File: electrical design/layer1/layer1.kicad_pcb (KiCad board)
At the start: 2 copper layers, 178 x 169.1 mm, 191 parts, among them J1 XT60-F, J2 1x07 2.54 FEMALE, J3 1x07 2.54 FEMALE, Q1 MOSFET-NCH-FQP30N06L, Q2 MOSFET-NCH-AO3404A, SW1 SW_DPDT_x2, U1 CD74HC4067SM, U2 CD74HC4067SM

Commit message: update layer 1 pcb
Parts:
- removed the C33 at (235.0, 105.0)
- removed the C33 at (-20.5, 99.5)
- removed the C34 at (224.9, 114.3)
- removed the C34 at (-19.5, 120.5)
- removed the C35 at (228.9, 115.0)
- removed the C36 at (250.7, 90.6)
- removed D33: 1N4728, Diode_THT:D_DO-41_SOD81_P10.16mm_Horizontal
- removed D34: 1N5401, Diode_THT:D_DO-27_P15.24mm_Horizontal
- removed J1, SOLENOID1: XT60-F, Connector_AMASS:AMASS_XT30UPB-F_1x02_P5.0mm_Vertical
- removed the R33 at (107.2, 57.8)
- removed the R33 at (-19.5, 122.2)
- removed the R35 at (-19.5, 124.0)
- removed the R35 at (156.0, 160.8)
- added C33: 1000µF/63V, Capacitor_THT:CP_Radial_D16.0mm_P7.50mm, F.Cu at (28.0, 89.2)
- added C34: 1500pF, Capacitor_SMD:C_0603_1608Metric, F.Cu at (28.5, 113.8)
- added H1: MountingHole, MountingHole:MountingHole_3.2mm_M3_Pad, F.Cu at (186.0, 44.0)
- added H10: MountingHole, MountingHole:MountingHole_3.2mm_M3_Pad, F.Cu at (209.8, 36.8)
- added H11: MountingHole, MountingHole:MountingHole_3.2mm_M3_Pad, F.Cu at (201.9, 52.6)
- added H12: MountingHole, MountingHole:MountingHole_3.2mm_M3_Pad, F.Cu at (217.8, 36.8)
- added H13: MountingHole, MountingHole:MountingHole_3.2mm_M3_Pad, F.Cu at (198.2, 28.8)
- added H14: MountingHole, MountingHole:MountingHole_3.2mm_M3_Pad, F.Cu at (222.1, 28.8)
- added H15: MountingHole, MountingHole:MountingHole_3.2mm_M3_Pad, F.Cu at (186.0, 36.0)
- added H16: MountingHole, MountingHole:MountingHole_3.2mm_M3_Pad, F.Cu at (193.9, 36.8)
- added H17: MountingHole, MountingHole:MountingHole_3.2mm_M3_Pad, F.Cu at (217.8, 44.7)
- added H18: MountingHole, MountingHole:MountingHole_3.2mm_M3_Pad, F.Cu at (214.2, 28.8)
- added H19: MountingHole, MountingHole:MountingHole_3.2mm_M3_Pad, F.Cu at (193.9, 52.6)
- added H2: MountingHole, MountingHole:MountingHole_3.2mm_M3_Pad, F.Cu at (186.0, 52.0)
- added H20: MountingHole, MountingHole:MountingHole_3.2mm_M3_Pad, F.Cu at (201.9, 44.7)
- added H21: MountingHole, MountingHole:MountingHole_3.2mm_M3_Pad, F.Cu at (201.9, 36.8)
- added H22: MountingHole, MountingHole:MountingHole_3.2mm_M3_Pad, F.Cu at (209.8, 52.6)
- added H3: MountingHole, MountingHole:MountingHole_3.2mm_M3_Pad, F.Cu at (230.1, 28.8)
- added H4: MountingHole, MountingHole:MountingHole_3.2mm_M3_Pad, F.Cu at (238.0, 28.8)
- added H5: MountingHole, MountingHole:MountingHole_3.2mm_M3_Pad, F.Cu at (206.2, 28.8)
- added H6: MountingHole, MountingHole:MountingHole_3.2mm_M3_Pad, F.Cu at (225.8, 36.8)
- added H7: MountingHole, MountingHole:MountingHole_3.2mm_M3_Pad, F.Cu at (217.8, 52.6)
- added H8: MountingHole, MountingHole:MountingHole_3.2mm_M3_Pad, F.Cu at (209.8, 44.7)
- added H9: MountingHole, MountingHole:MountingHole_3.2mm_M3_Pad, F.Cu at (72.1, 59.1)
- added J4: XT30PW-F, Connector_AMASS:AMASS_XT30PW-F_1x02_P2.50mm_Horizontal, F.Cu at (43.4, 102.5)
- added R33: 20, Resistor_SMD:R_0603_1608Metric, F.Cu at (28.5, 115.5)
- added R35: 10k, Resistor_SMD:R_0603_1608Metric, F.Cu at (28.5, 117.2)
- C35: renamed from C36; moved to B.Cu
- C36: renamed from C37; moved to B.Cu
- R36, R37, R38, R39, U1, U2: moved to B.Cu
- moved D2 196.8 mm to (35.0, 104.8), turned to -90 degrees
- moved D1 172.7 mm to (38.5, 104.1), turned to 90 degrees
- moved C36 64.5 mm to (143.5, 100.8), turned to -90 degrees
- moved C35 64.2 mm to (67.0, 109.3), turned to 90 degrees
- moved R38 52.5 mm to (143.5, 109.2), turned to 90 degrees
- moved R36 51.8 mm to (67.0, 100.5), turned to -90 degrees
- moved Q1 46.4 mm to (29.0, 109.8), turned to 90 degrees
- moved U2 45.8 mm to (134.5, 105.0), turned to 90 degrees
- moved U1 45.5 mm to (76.0, 105.0), turned to -90 degrees
- moved J2 43.8 mm to (230.8, 98.9)
- moved J3 43.8 mm to (230.8, 115.1)
- moved SW1 43.8 mm to (226.8, 120.0)
- moved R39 37.3 mm to (123.5, 100.0), turned to 180 degrees
- moved R37 37.0 mm to (87.0, 110.0), turned to 0 degrees
- moved R34 35.5 mm to (28.5, 119.0)
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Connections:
- D1 pad 2: /SOLENOIDPOWER -> +48V
- LDR10 pad 1: unconnected-(LDR10-Pad1) -> VCCQ
- LDR11 pad 1: unconnected-(LDR11-Pad1) -> VCCQ
- LDR12 pad 1: unconnected-(LDR12-Pad1) -> VCCQ
- LDR13 pad 1: unconnected-(LDR13-Pad1) -> VCCQ
- LDR14 pad 1: unconnected-(LDR14-Pad1) -> VCCQ
- LDR15 pad 1: unconnected-(LDR15-Pad1) -> VCCQ
- LDR16 pad 1: unconnected-(LDR16-Pad1) -> VCCQ
- LDR17 pad 1: unconnected-(LDR17-Pad1) -> VCCQ
- LDR17 pad 2: unconnected-(LDR17-Pad2) -> Net-(LDR17-Pad2)
- LDR18 pad 1: unconnected-(LDR18-Pad1) -> VCCQ
- LDR18 pad 2: unconnected-(LDR18-Pad2) -> Net-(LDR18-Pad2)
- LDR19 pad 1: unconnected-(LDR19-Pad1) -> VCCQ
- LDR19 pad 2: unconnected-(LDR19-Pad2) -> Net-(LDR19-Pad2)
- LDR20 pad 1: unconnected-(LDR20-Pad1) -> VCCQ
- LDR20 pad 2: unconnected-(LDR20-Pad2) -> Net-(LDR20-Pad2)
- LDR21 pad 1: unconnected-(LDR21-Pad1) -> VCCQ
- LDR21 pad 2: unconnected-(LDR21-Pad2) -> Net-(LDR21-Pad2)
- LDR22 pad 1: unconnected-(LDR22-Pad1) -> VCCQ
- LDR22 pad 2: unconnected-(LDR22-Pad2) -> Net-(LDR22-Pad2)
- LDR23 pad 1: unconnected-(LDR23-Pad1) -> VCCQ
- LDR23 pad 2: unconnected-(LDR23-Pad2) -> Net-(LDR23-Pad2)
- LDR24 pad 1: unconnected-(LDR24-Pad1) -> VCCQ
- LDR24 pad 2: unconnected-(LDR24-Pad2) -> Net-(LDR24-Pad2)
- LDR25 pad 1: unconnected-(LDR25-Pad1) -> VCCQ
- LDR25 pad 2: unconnected-(LDR25-Pad2) -> Net-(LDR25-Pad2)
- LDR26 pad 1: unconnected-(LDR26-Pad1) -> VCCQ
- LDR26 pad 2: unconnected-(LDR26-Pad2) -> Net-(LDR26-Pad2)
- LDR27 pad 1: unconnected-(LDR27-Pad1) -> VCCQ
- LDR27 pad 2: unconnected-(LDR27-Pad2) -> Net-(LDR27-Pad2)
- LDR28 pad 1: unconnected-(LDR28-Pad1) -> VCCQ
- LDR28 pad 2: unconnected-(LDR28-Pad2) -> Net-(LDR28-Pad2)
- LDR29 pad 1: unconnected-(LDR29-Pad1) -> VCCQ
- LDR29 pad 2: unconnected-(LDR29-Pad2) -> Net-(LDR29-Pad2)
- LDR30 pad 1: unconnected-(LDR30-Pad1) -> VCCQ
- LDR30 pad 2: unconnected-(LDR30-Pad2) -> Net-(LDR30-Pad2)
- LDR31 pad 1: unconnected-(LDR31-Pad1) -> VCCQ
- LDR31 pad 2: unconnected-(LDR31-Pad2) -> Net-(LDR31-Pad2)
- LDR32 pad 1: unconnected-(LDR32-Pad1) -> VCCQ
- LDR32 pad 2: unconnected-(LDR32-Pad2) -> Net-(LDR32-Pad2)
- LDR9 pad 1: unconnected-(LDR9-Pad1) -> VCCQ
- R34 pad 1: Net-(R34-Pad1) -> +12V
- U1 pad 16: unconnected-(U1-Pad16) -> Net-(LDR16-Pad2)
- U1 pad 17: unconnected-(U1-Pad17) -> Net-(LDR15-Pad2)
- U1 pad 18: unconnected-(U1-Pad18) -> Net-(LDR14-Pad2)
- U1 pad 19: unconnected-(U1-Pad19) -> Net-(LDR13-Pad2)
- U1 pad 2: Net-(LDR1-Pad2) -> Net-(LDR8-Pad2)
- U1 pad 20: unconnected-(U1-Pad20) -> Net-(LDR12-Pad2)
- U1 pad 21: unconnected-(U1-Pad21) -> Net-(LDR11-Pad2)
- U1 pad 22: unconnected-(U1-Pad22) -> Net-(LDR10-Pad2)
- U1 pad 23: unconnected-(U1-Pad23) -> Net-(LDR9-Pad2)
- U1 pad 3: Net-(LDR2-Pad2) -> Net-(LDR7-Pad2)
- U1 pad 4: Net-(LDR3-Pad2) -> Net-(LDR6-Pad2)
- U1 pad 5: Net-(LDR4-Pad2) -> Net-(LDR5-Pad2)
- U1 pad 6: Net-(LDR5-Pad2) -> Net-(LDR4-Pad2)
- U1 pad 7: Net-(LDR6-Pad2) -> Net-(LDR3-Pad2)
- U1 pad 8: Net-(LDR7-Pad2) -> Net-(LDR2-Pad2)
- U1 pad 9: Net-(LDR8-Pad2) -> Net-(LDR1-Pad2)
- U2 pad 16: Net-(LDR9-Pad2) -> Net-(LDR32-Pad2)
- U2 pad 17: Net-(LDR10-Pad2) -> Net-(LDR31-Pad2)
- U2 pad 18: Net-(LDR11-Pad2) -> Net-(LDR30-Pad2)
- U2 pad 19: Net-(LDR12-Pad2) -> Net-(LDR29-Pad2)
- U2 pad 2: unconnected-(U2-Pad2) -> Net-(LDR24-Pad2)
- U2 pad 20: Net-(LDR13-Pad2) -> Net-(LDR28-Pad2)
- U2 pad 21: Net-(LDR14-Pad2) -> Net-(LDR27-Pad2)
- U2 pad 22: Net-(LDR15-Pad2) -> Net-(LDR26-Pad2)
- U2 pad 23: Net-(LDR16-Pad2) -> Net-(LDR25-Pad2)
- U2 pad 3: unconnected-(U2-Pad3) -> Net-(LDR23-Pad2)
- U2 pad 4: unconnected-(U2-Pad4) -> Net-(LDR22-Pad2)
- U2 pad 5: unconnected-(U2-Pad5) -> Net-(LDR21-Pad2)
- U2 pad 6: unconnected-(U2-Pad6) -> Net-(LDR20-Pad2)
- U2 pad 7: unconnected-(U2-Pad7) -> Net-(LDR19-Pad2)
- U2 pad 8: unconnected-(U2-Pad8) -> Net-(LDR18-Pad2)
- U2 pad 9: unconnected-(U2-Pad9) -> Net-(LDR17-Pad2)
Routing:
- net +3V3: track 183.3 -> 4.59 mm, vias 3 -> 0
- net /MUX1OUT: track 113.0 -> 2.47 mm, vias 2 -> 0
- net /MUX2OUT: track 104.5 -> 2.19 mm, vias 2 -> 0
- net /S0: track 69.0 -> 0.00 mm, vias 2 -> 0
- net /S1: track 66.4 -> 0.00 mm, vias 2 -> 0
- net /S2: track 65.5 -> 0.00 mm, vias 2 -> 0
- net /S3: track 63.2 -> 0.00 mm, vias 2 -> 0
- net unconnected-(LDR25-Pad2): track 60.5 -> 0.00 mm, vias 1 -> 0
- net unconnected-(LDR24-Pad2): track 60.5 -> 0.00 mm, vias 1 -> 0
- net Net-(LDR8-Pad2): track 60.5 -> 3.33 mm, vias 1 -> 2
- net Net-(LDR9-Pad2): track 60.5 -> 3.33 mm, vias 1 -> 2
- net unconnected-(LDR26-Pad2): track 55.1 -> 0.00 mm, vias 1 -> 0
- net unconnected-(U2-Pad8): track 54.9 -> 0.00 mm, vias 1 -> 0
- net Net-(LDR7-Pad2): track 54.9 -> 3.34 mm, vias 1 -> 2
- net Net-(LDR10-Pad2): track 54.9 -> 3.34 mm, vias 1 -> 2
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- added copper zone on F.Cu, net +48V
- added copper zone on F.Cu, net Net-(D1-Pad1)
- added copper zone on B.Cu, net Net-(D2-Pad2)
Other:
- board size 178 x 169.1 mm -> 178 x 168.1 mm
- board text added: "BOOST"
- board text added: "KICKER"
- board text added: "SOLENOID-1039"
- board text added: "SOLENOID-1040"
- board text added: "ducc."

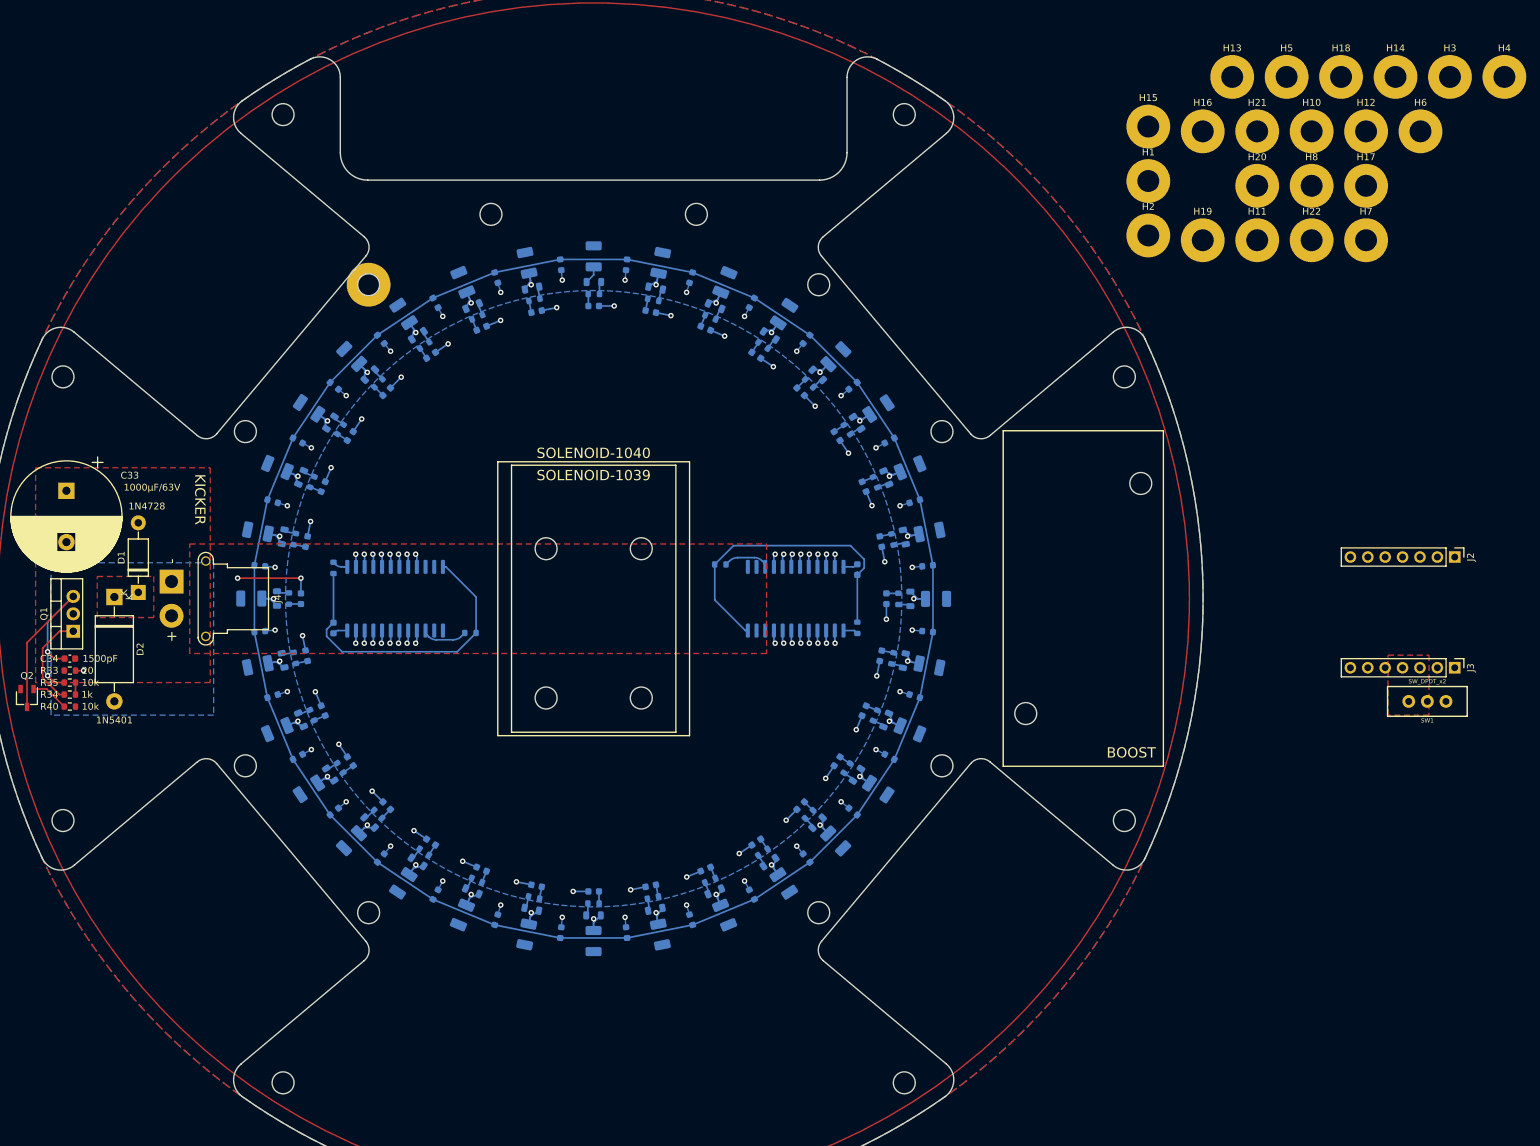
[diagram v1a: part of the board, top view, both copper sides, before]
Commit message: placed layer 1 mounting holes
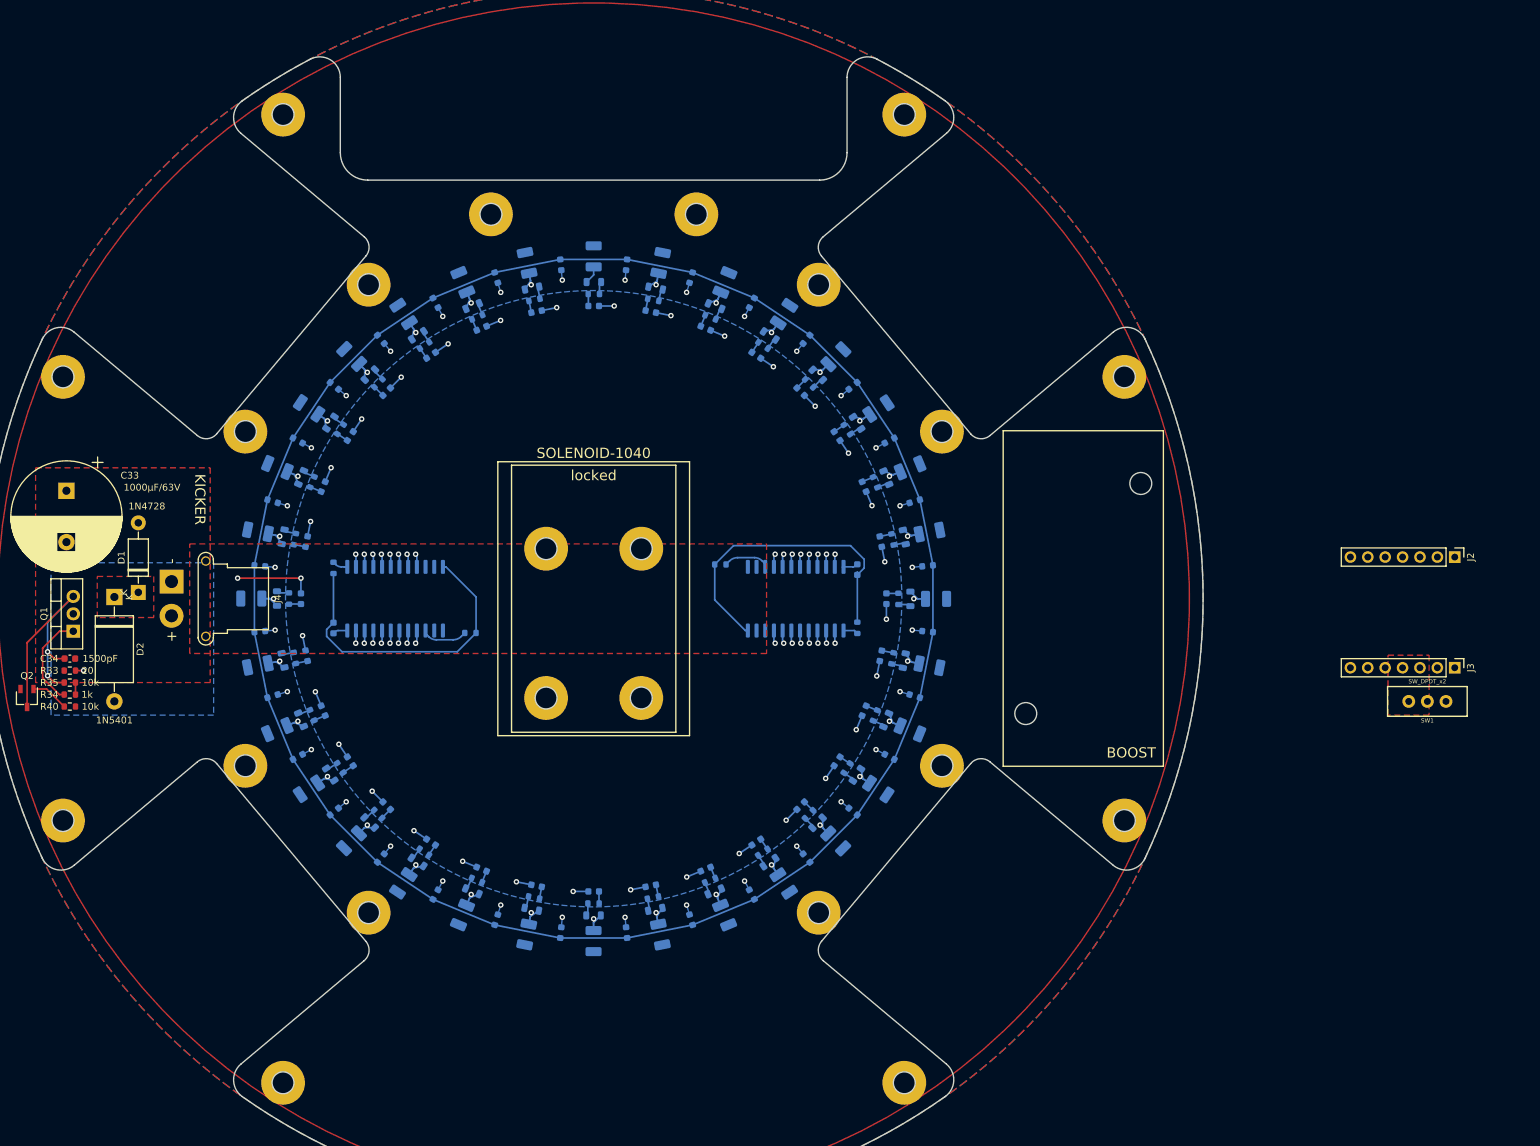
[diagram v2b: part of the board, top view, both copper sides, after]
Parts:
- moved H14 219.0 mm to (59.6, 175.7)
- moved H3 199.6 mm to (72.1, 150.9)
- moved H20 197.5 mm to (27.5, 137.4)
- moved H4 171.1 mm to (150.4, 175.7)
- moved H11 166.5 mm to (54.1, 129.4)
- moved H1 161.1 mm to (27.5, 72.6)
- moved H10 150.2 mm to (59.6, 34.3)
- moved H16 146.5 mm to (54.1, 80.6)
- moved H6 144.0 mm to (137.9, 150.9)
- moved H17 141.2 mm to (98.0, 119.5)
- moved H12 134.4 mm to (112.0, 119.5)
- moved H8 123.7 mm to (98.0, 97.7)
- moved H7 115.0 mm to (112.0, 97.7)
- moved H13 110.1 mm to (90.0, 48.9)
- moved H22 93.8 mm to (155.9, 129.4)
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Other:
- board text added: "locked"
- board text removed: "SOLENOID-1039"
